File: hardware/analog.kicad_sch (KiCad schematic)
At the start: 11 parts, among them J1 Conn_01x02, U1 ${SIM.PARAMS}, U2 ${SIM.PARAMS}, U3 ${SIM.PARAMS}

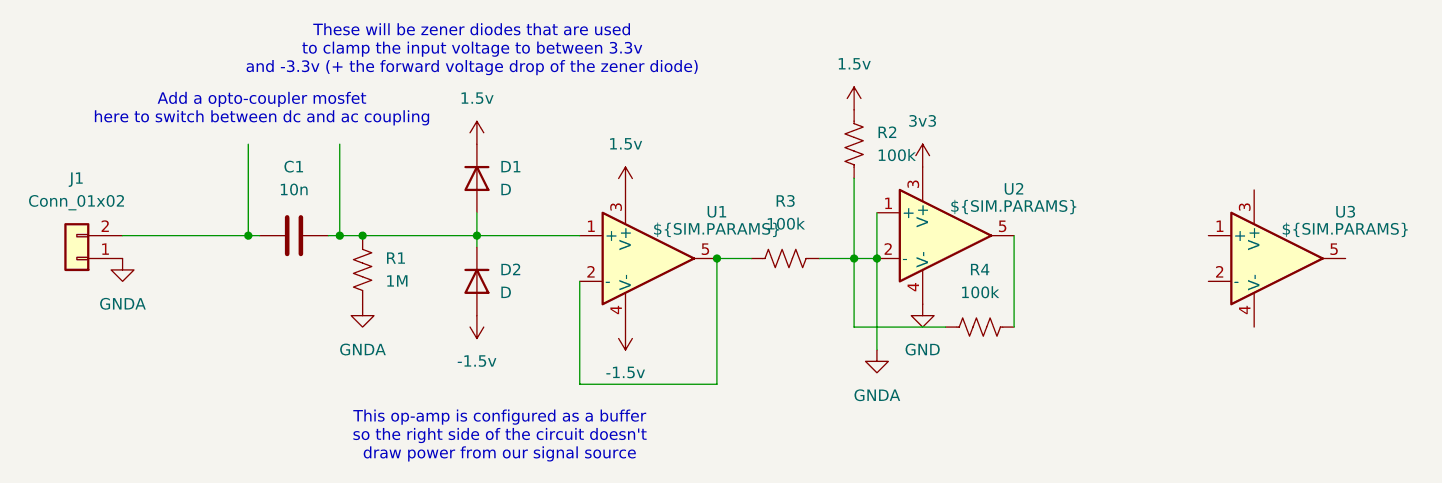
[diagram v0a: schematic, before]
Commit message: feat(hardware): Add 8MB PSRAM Flash
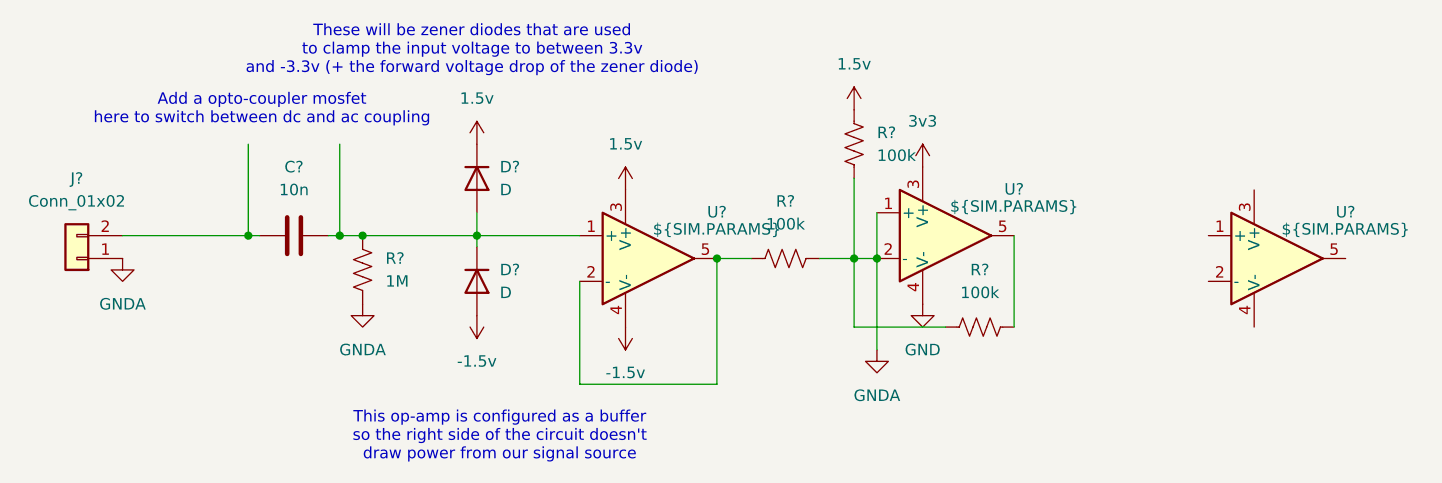
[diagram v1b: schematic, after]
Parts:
- renumbered C1 to C?, D1 to D?, D2 to D?, J1 to J?, R2 to R?, R4 to R?, R3 to R?, R1 to R?, U1 to U?, U3 to U?, U2 to U?
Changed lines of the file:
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@@
 		(dnp no)
 		(fields_autoplaced yes)
-		(property "Reference" "D1"
+		(property "Reference" "D?"
 			(at 81.28 59.6899 90)
 			(effects
@@
 		)
 		(instances
+			(project "RP2350_60QFN_minimal"
+				(path "/94683f5c-9cd9-448e-be96-9792537b5cb8/73c3c5fb-df78-41b9-8072-c8773a39fe38"
+					(reference "D?")
+					(unit 1)
+				)
+			)
 			(project ""
 				(path "/cad06ff6-1510-49dc-9cf8-644755c75ad2"
@@
 		(dnp no)
 		(fields_autoplaced yes)
-		(property "Reference" "#PWR02"
+		(property "Reference" "#PWR?"
 			(at 66.04 81.28 0)
 			(effects
@@
 		)
 		(instances
+			(project "RP2350_60QFN_minimal"
+				(path "/94683f5c-9cd9-448e-be96-9792537b5cb8/73c3c5fb-df78-41b9-8072-c8773a39fe38"
+					(reference "#PWR?")
+					(unit 1)
+				)
+			)
 			(project "analog"
 				(path "/cad06ff6-1510-49dc-9cf8-644755c75ad2"
@@
 		(dnp no)
 		(fields_autoplaced yes)
-		(property "Reference" "#PWR03"
+		(property "Reference" "#PWR?"
 			(at 78.74 60.96 0)
 			(effects
@@
 		)
 		(instances
+			(project "RP2350_60QFN_minimal"
+				(path "/94683f5c-9cd9-448e-be96-9792537b5cb8/73c3c5fb-df78-41b9-8072-c8773a39fe38"
+					(reference "#PWR?")
+					(unit 1)
+				)
+			)
 			(project ""
 				(path "/cad06ff6-1510-49dc-9cf8-644755c75ad2"
@@
 		(dnp no)
 		(fields_autoplaced yes)
-		(property "Reference" "U1"
+		(property "Reference" "U?"
 			(at 105.41 64.6998 0)
 			(effects
@@
 		)
 		(instances
+			(project "RP2350_60QFN_minimal"
+				(path "/94683f5c-9cd9-448e-be96-9792537b5cb8/73c3c5fb-df78-41b9-8072-c8773a39fe38"
+					(reference "U?")
+					(unit 1)
+				)
+			)
 			(project ""
 				(path "/cad06ff6-1510-49dc-9cf8-644755c75ad2"
@@
 		(dnp no)
 		(fields_autoplaced yes)
-		(property "Reference" "U3"
+		(property "Reference" "U?"
 			(at 175.26 64.6998 0)
 			(effects
@@
 		)
 		(instances
+			(project "RP2350_60QFN_minimal"
+				(path "/94683f5c-9cd9-448e-be96-9792537b5cb8/73c3c5fb-df78-41b9-8072-c8773a39fe38"
+					(reference "U?")
+					(unit 1)
+				)
+			)
 			(project "analog"
 				(path "/cad06ff6-1510-49dc-9cf8-644755c75ad2"
@@
 		(dnp no)
 		(fields_autoplaced yes)
-		(property "Reference" "U2"
+		(property "Reference" "U?"
 			(at 138.43 62.1598 0)
 			(effects
@@
 		)
 		(instances
+			(project "RP2350_60QFN_minimal"
+				(path "/94683f5c-9cd9-448e-be96-9792537b5cb8/73c3c5fb-df78-41b9-8072-c8773a39fe38"
+					(reference "U?")
+					(unit 1)
+				)
+			)
 			(project "analog"
 				(path "/cad06ff6-1510-49dc-9cf8-644755c75ad2"
@@
 		(dnp no)
 		(fields_autoplaced yes)
-		(property "Reference" "C1"
+		(property "Reference" "C?"
 			(at 58.42 59.69 90)
 			(effects
@@
 		)
 		(instances
+			(project "RP2350_60QFN_minimal"
+				(path "/94683f5c-9cd9-448e-be96-9792537b5cb8/73c3c5fb-df78-41b9-8072-c8773a39fe38"
+					(reference "C?")
+					(unit 1)
+				)
+			)
 			(project ""
 				(path "/cad06ff6-1510-49dc-9cf8-644755c75ad2"
@@
 		(dnp no)
 		(fields_autoplaced yes)
-		(property "Reference" "#PWR06"
+		(property "Reference" "#PWR?"
 			(at 95.25 73.66 0)
 			(effects
@@
 		)
 		(instances
+			(project "RP2350_60QFN_minimal"
+				(path "/94683f5c-9cd9-448e-be96-9792537b5cb8/73c3c5fb-df78-41b9-8072-c8773a39fe38"
+					(reference "#PWR?")
+					(unit 1)
+				)
+			)
 			(project "analog"
 				(path "/cad06ff6-1510-49dc-9cf8-644755c75ad2"
@@
 		(dnp no)
 		(fields_autoplaced yes)
-		(property "Reference" "R2"
+		(property "Reference" "R?"
 			(at 123.19 55.8799 0)
 			(effects
@@
 		)
 		(instances
+			(project "RP2350_60QFN_minimal"
+				(path "/94683f5c-9cd9-448e-be96-9792537b5cb8/73c3c5fb-df78-41b9-8072-c8773a39fe38"
+					(reference "R?")
+					(unit 1)
+				)
+			)
 			(project ""
 				(path "/cad06ff6-1510-49dc-9cf8-644755c75ad2"
@@
 		(dnp no)
 		(fields_autoplaced yes)
-		(property "Reference" "R4"
+		(property "Reference" "R?"
 			(at 134.62 71.12 90)
 			(effects
@@
 		)
 		(instances
+			(project "RP2350_60QFN_minimal"
+				(path "/94683f5c-9cd9-448e-be96-9792537b5cb8/73c3c5fb-df78-41b9-8072-c8773a39fe38"
+					(reference "R?")
+					(unit 1)
+				)
+			)
 			(project "analog"
 				(path "/cad06ff6-1510-49dc-9cf8-644755c75ad2"
@@
 		(dnp no)
 		(fields_autoplaced yes)
-		(property "Reference" "R3"
+		(property "Reference" "R?"
 			(at 113.03 63.5 90)
 			(effects
@@
 		)
 		(instances
+			(project "RP2350_60QFN_minimal"
+				(path "/94683f5c-9cd9-448e-be96-9792537b5cb8/73c3c5fb-df78-41b9-8072-c8773a39fe38"
+					(reference "R?")
+					(unit 1)
+				)
+			)
 			(project "analog"
 				(path "/cad06ff6-1510-49dc-9cf8-644755c75ad2"
@@
 		(dnp no)
 		(fields_autoplaced yes)
-		(property "Reference" "D2"
+		(property "Reference" "D?"
 			(at 81.28 71.1199 90)
 			(effects
@@
 		)
 		(instances
+			(project "RP2350_60QFN_minimal"
+				(path "/94683f5c-9cd9-448e-be96-9792537b5cb8/73c3c5fb-df78-41b9-8072-c8773a39fe38"
+					(reference "D?")
+					(unit 1)
+				)
+			)
 			(project "analog"
 				(path "/cad06ff6-1510-49dc-9cf8-644755c75ad2"
@@
 		(dnp no)
 		(fields_autoplaced yes)
-		(property "Reference" "R1"
+		(property "Reference" "R?"
 			(at 68.58 69.8499 0)
 			(effects
@@
 		)
 		(instances
+			(project "RP2350_60QFN_minimal"
+				(path "/94683f5c-9cd9-448e-be96-9792537b5cb8/73c3c5fb-df78-41b9-8072-c8773a39fe38"
+					(reference "R?")
+					(unit 1)
+				)
+			)
 			(project ""
 				(path "/cad06ff6-1510-49dc-9cf8-644755c75ad2"
@@
 		(dnp no)
 		(fields_autoplaced yes)
-		(property "Reference" "#PWR08"
+		(property "Reference" "#PWR?"
 			(at 120.65 57.15 0)
 			(effects
@@
 		)
 		(instances
+			(project "RP2350_60QFN_minimal"
+				(path "/94683f5c-9cd9-448e-be96-9792537b5cb8/73c3c5fb-df78-41b9-8072-c8773a39fe38"
+					(reference "#PWR?")
+					(unit 1)
+				)
+			)
 			(project "analog"
 				(path "/cad06ff6-1510-49dc-9cf8-644755c75ad2"
@@
 		(dnp no)
 		(fields_autoplaced yes)
-		(property "Reference" "#PWR010"
+		(property "Reference" "#PWR?"
 			(at 128.27 81.28 0)
 			(effects
@@
 		)
 		(instances
+			(project "RP2350_60QFN_minimal"
+				(path "/94683f5c-9cd9-448e-be96-9792537b5cb8/73c3c5fb-df78-41b9-8072-c8773a39fe38"
+					(reference "#PWR?")
+					(unit 1)
+				)
+			)
 			(project "analog"
 				(path "/cad06ff6-1510-49dc-9cf8-644755c75ad2"
@@
 		(dnp no)
 		(fields_autoplaced yes)
-		(property "Reference" "#PWR09"
+		(property "Reference" "#PWR?"
 			(at 128.27 63.5 0)
 			(effects
@@
 		)
 		(instances
+			(project "RP2350_60QFN_minimal"
+				(path "/94683f5c-9cd9-448e-be96-9792537b5cb8/73c3c5fb-df78-41b9-8072-c8773a39fe38"
+					(reference "#PWR?")
+					(unit 1)
+				)
+			)
 			(project "analog"
 				(path "/cad06ff6-1510-49dc-9cf8-644755c75ad2"
@@
 		(dnp no)
 		(fields_autoplaced yes)
-		(property "Reference" "#PWR04"
+		(property "Reference" "#PWR?"
 			(at 78.74 72.39 0)
 			(effects
@@
 		)
 		(instances
+			(project "RP2350_60QFN_minimal"
+				(path "/94683f5c-9cd9-448e-be96-9792537b5cb8/73c3c5fb-df78-41b9-8072-c8773a39fe38"
+					(reference "#PWR?")
+					(unit 1)
+				)
+			)
 			(project ""
 				(path "/cad06ff6-1510-49dc-9cf8-644755c75ad2"
@@
 		(dnp no)
 		(fields_autoplaced yes)
-		(property "Reference" "#PWR01"
+		(property "Reference" "#PWR?"
 			(at 39.37 76.2 0)
 			(effects
@@
 		)
 		(instances
+			(project "RP2350_60QFN_minimal"
+				(path "/94683f5c-9cd9-448e-be96-9792537b5cb8/73c3c5fb-df78-41b9-8072-c8773a39fe38"
+					(reference "#PWR?")
+					(unit 1)
+				)
+			)
 			(project ""
 				(path "/cad06ff6-1510-49dc-9cf8-644755c75ad2"
@@
 		(dnp no)
 		(fields_autoplaced yes)
-		(property "Reference" "J1"
+		(property "Reference" "J?"
 			(at 34.29 60.96 0)
 			(effects
@@
 		)
 		(instances
+			(project "RP2350_60QFN_minimal"
+				(path "/94683f5c-9cd9-448e-be96-9792537b5cb8/73c3c5fb-df78-41b9-8072-c8773a39fe38"
+					(reference "J?")
+					(unit 1)
+				)
+			)
 			(project ""
 				(path "/cad06ff6-1510-49dc-9cf8-644755c75ad2"
@@
 		(dnp no)
 		(fields_autoplaced yes)
-		(property "Reference" "#PWR05"
+		(property "Reference" "#PWR?"
 			(at 95.25 66.04 0)
 			(effects
@@
 		)
 		(instances
+			(project "RP2350_60QFN_minimal"
+				(path "/94683f5c-9cd9-448e-be96-9792537b5cb8/73c3c5fb-df78-41b9-8072-c8773a39fe38"
+					(reference "#PWR?")
+					(unit 1)
+				)
+			)
 			(project "analog"
 				(path "/cad06ff6-1510-49dc-9cf8-644755c75ad2"
@@
 		(dnp no)
 		(fields_autoplaced yes)
-		(property "Reference" "#PWR07"
+		(property "Reference" "#PWR?"
 			(at 123.19 86.36 0)
 			(effects
@@
 		)
 		(instances
+			(project "RP2350_60QFN_minimal"
+				(path "/94683f5c-9cd9-448e-be96-9792537b5cb8/73c3c5fb-df78-41b9-8072-c8773a39fe38"
+					(reference "#PWR?")
+					(unit 1)
+				)
+			)
 			(project "analog"
 				(path "/cad06ff6-1510-49dc-9cf8-644755c75ad2"

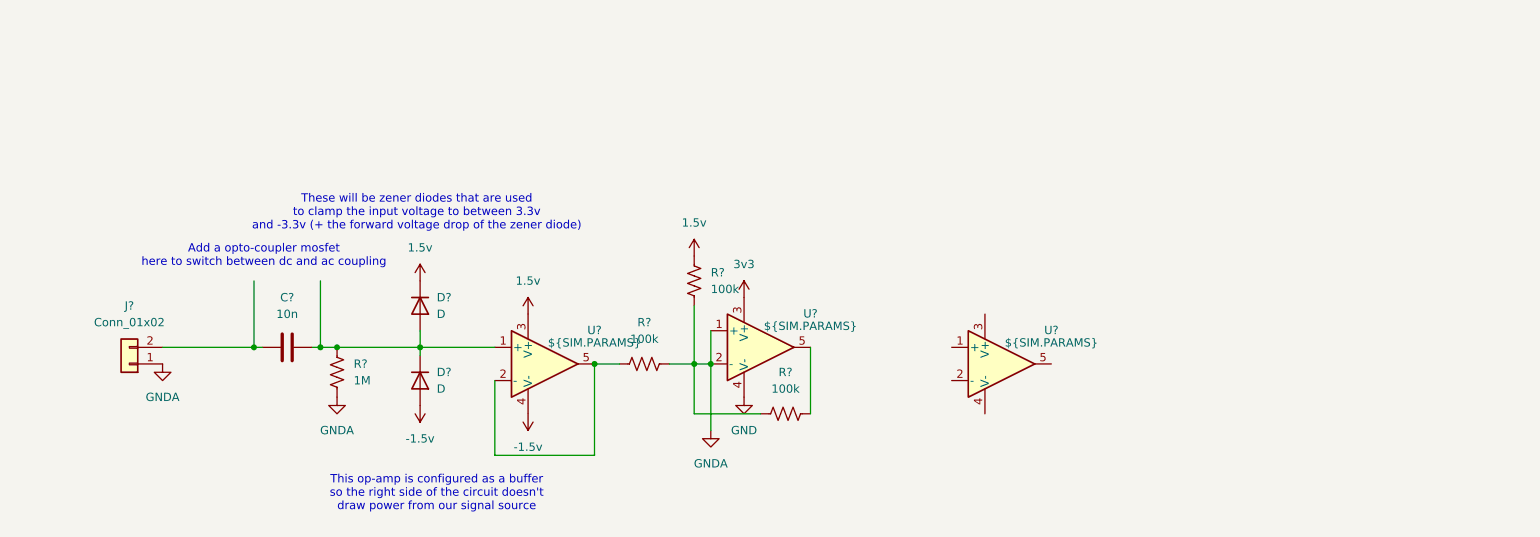
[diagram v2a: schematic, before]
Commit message: added heirarchical labels for analog block
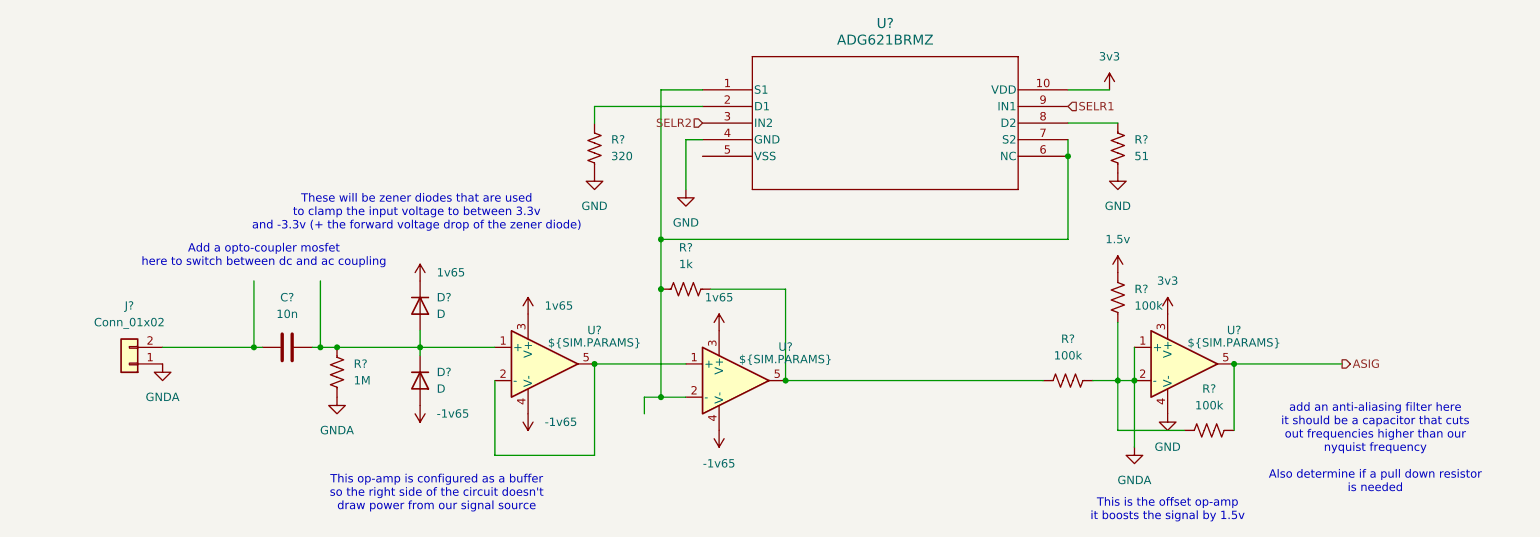
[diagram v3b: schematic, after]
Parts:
- added R?: 320, symbol Device:R_US
- added R?: 1k, symbol Device:R_US
- added R?: 51, symbol Device:R_US
- added U?: ADG621BRMZ, RM_10_ADI, symbol ADG621BRMZ (switch):ADG621BRMZ
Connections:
- net -1.5v is gone; now on net -1v65: D?.2 (A), U?.4 (V-)
- net 1.5v: no longer D?.1 (K), U?.3 (V+)
- net 3v3: now also U?.10 (VDD)
- net GND: now also R?.1, R?.1, U?.4 (GND)
- net at U?.2 (-), U?.5: now also U?.1 (+); no longer R?.2
- net at U?.2 (-): now also R?.1, U?.1 (S1), U?.6 (NC), U?.7 (S2)
- net 1v65: now reaches U?.3 (V+)
- net 1v65: now also D?.1 (K), U?.3 (V+)
- net -1v65: now reaches U?.4 (V-)
- net at U?.5: now also R?.2, R?.2
- net ASIG: now reaches R?.1, U?.5
- new net: R?.2, U?.2 (D1)
- new net: R?.2, U?.8 (D2)
- new net SELR1: U?.9 (IN1)
- new net SELR2: U?.3 (IN2)
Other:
- note added: "This is the offset op-amp it boosts the signal by 1.5v"
- note added: "add an anti-aliasing filter here it should be a capacitor that cuts out frequencies higher than our nyquist frequency Also determine if a pull down resistor is needed"
- moved on the sheet: R?, U?

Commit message: merging stuff
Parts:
- gave numbers to parts that had none: 15
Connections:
- net GND: no longer U4.4 (GND)
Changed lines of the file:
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@@
 		(dnp no)
 		(fields_autoplaced yes)
-		(property "Reference" "#PWR?"
+		(property "Reference" "#PWR014"
 			(at 124.46 68.58 0)
 			(effects
@@
 		(dnp no)
 		(fields_autoplaced yes)
-		(property "Reference" "D?"
+		(property "Reference" "D1"
 			(at 81.28 59.6899 90)
 			(effects
@@
 		(dnp no)
 		(fields_autoplaced yes)
-		(property "Reference" "#PWR?"
+		(property "Reference" "#PWR02"
 			(at 66.04 81.28 0)
 			(effects
@@
 		(dnp no)
 		(fields_autoplaced yes)
-		(property "Reference" "R?"
+		(property "Reference" "R7"
 			(at 107.95 35.5599 0)
 			(effects
@@
 		(dnp no)
 		(fields_autoplaced yes)
-		(property "Reference" "#PWR?"
+		(property "Reference" "#PWR03"
 			(at 78.74 60.96 0)
 			(effects
@@
 		(dnp no)
 		(fields_autoplaced yes)
-		(property "Reference" "U?"
+		(property "Reference" "U1"
 			(at 105.41 64.6998 0)
 			(effects
@@
 		(dnp no)
 		(fields_autoplaced yes)
-		(property "Reference" "U?"
+		(property "Reference" "U3"
 			(at 134.62 67.2398 0)
 			(effects
@@
 		(dnp no)
 		(fields_autoplaced yes)
-		(property "Reference" "U?"
+		(property "Reference" "U2"
 			(at 203.2 64.6998 0)
 			(effects
@@
 		(dnp no)
 		(fields_autoplaced yes)
-		(property "Reference" "C?"
+		(property "Reference" "C1"
 			(at 58.42 59.69 90)
 			(effects
@@
 		(dnp no)
 		(fields_autoplaced yes)
-		(property "Reference" "#PWR?"
+		(property "Reference" "#PWR06"
 			(at 95.25 73.66 0)
 			(effects
@@
 		(dnp no)
 		(fields_autoplaced yes)
-		(property "Reference" "R?"
+		(property "Reference" "R6"
 			(at 119.38 52.07 90)
 			(effects
@@
 		(dnp no)
 		(fields_autoplaced yes)
-		(property "Reference" "R?"
+		(property "Reference" "R2"
 			(at 187.96 58.4199 0)
 			(effects
@@
 		(dnp no)
 		(fields_autoplaced yes)
-		(property "Reference" "R?"
+		(property "Reference" "R4"
 			(at 199.39 73.66 90)
 			(effects
@@
 		(dnp no)
 		(fields_autoplaced yes)
-		(property "Reference" "#PWR?"
+		(property "Reference" "#PWR015"
 			(at 124.46 76.2 0)
 			(effects
@@
 		(dnp no)
 		(fields_autoplaced yes)
-		(property "Reference" "R?"
+		(property "Reference" "R3"
 			(at 177.8 66.04 90)
 			(effects
@@
 		(dnp no)
 		(fields_autoplaced yes)
-		(property "Reference" "D?"
+		(property "Reference" "D2"
 			(at 81.28 71.1199 90)
 			(effects
@@
 		(dnp no)
 		(fields_autoplaced yes)
-		(property "Reference" "R?"
+		(property "Reference" "R1"
 			(at 68.58 69.8499 0)
 			(effects
@@
 		(dnp no)
 		(fields_autoplaced yes)
-		(property "Reference" "#PWR?"
+		(property "Reference" "#PWR016"
 			(at 105.41 46.99 0)
 			(effects
@@
 		(dnp no)
 		(fields_autoplaced yes)
-		(property "Reference" "R?"
+		(property "Reference" "R8"
 			(at 187.96 35.5599 0)
 			(effects
@@
 		(dnp no)
 		(fields_autoplaced yes)
-		(property "Reference" "#PWR?"
+		(property "Reference" "#PWR08"
 			(at 185.42 59.69 0)
 			(effects
@@
 		(dnp no)
 		(fields_autoplaced yes)
-		(property "Reference" "#PWR?"
+		(property "Reference" "#PWR017"
 			(at 185.42 46.99 0)
 			(effects
@@
 		(dnp no)
 		(fields_autoplaced yes)
-		(property "Reference" "#PWR?"
+		(property "Reference" "#PWR010"
 			(at 193.04 83.82 0)
 			(effects
@@
 		(dnp no)
 		(fields_autoplaced yes)
-		(property "Reference" "U?"
+		(property "Reference" "U4"
 			(at 149.86 17.78 0)
 			(effects
@@
 	)
 	(symbol
-		(lib_id "power:GND")
-		(at 119.38 43.18 0)
-		(unit 1)
-		(exclude_from_sim no)
-		(in_bom yes)
-		(on_board yes)
-		(dnp no)
-		(fields_autoplaced yes)
-		(property "Reference" "#PWR?"
-			(at 119.38 49.53 0)
-			(effects
-				(font
-					(size 1.27 1.27)
-				)
-				(hide yes)
-			)
-		)
-		(property "Value" "GND"
-			(at 119.38 48.26 0)
-			(effects
-				(font
-					(size 1.27 1.27)
-				)
-			)
-		)
-		(property "Footprint" ""
-			(at 119.38 43.18 0)
-			(effects
-				(font
-					(size 1.27 1.27)
-				)
-				(hide yes)
-			)
-		)
-		(property "Datasheet" ""
-			(at 119.38 43.18 0)
-			(effects
-				(font
-					(size 1.27 1.27)
-				)
-				(hide yes)
-			)
-		)
-		(property "Description" "Power symbol creates a global label with name \"GND\" , ground"
-			(at 119.38 43.18 0)
-			(effects
-				(font
-					(size 1.27 1.27)
-				)
-				(hide yes)
-			)
-		)
-		(pin "1"
-		)
-		(instances
-			(project "RP2350_60QFN_minimal"
-				(path "/94683f5c-9cd9-448e-be96-9792537b5cb8/73c3c5fb-df78-41b9-8072-c8773a39fe38"
-					(reference "#PWR?")
-					(unit 1)
-				)
-			)
-			(project "analog"
-				(path "/cad06ff6-1510-49dc-9cf8-644755c75ad2"
-					(reference "#PWR013")
-					(unit 1)
-				)
-			)
-		)
-	)
-	(symbol
 		(lib_id "power:VDC")
 		(at 193.04 62.23 0)
@@
 		(dnp no)
 		(fields_autoplaced yes)
-		(property "Reference" "#PWR?"
+		(property "Reference" "#PWR09"
 			(at 193.04 66.04 0)
 			(effects
@@
 		(dnp no)
 		(fields_autoplaced yes)
-		(property "Reference" "#PWR?"
+		(property "Reference" "#PWR04"
 			(at 78.74 72.39 0)
 			(effects
@@
 		(dnp no)
 		(fields_autoplaced yes)
-		(property "Reference" "#PWR?"
+		(property "Reference" "#PWR01"
 			(at 39.37 76.2 0)
 			(effects
@@
 		(dnp no)
 		(fields_autoplaced yes)
-		(property "Reference" "J?"
+		(property "Reference" "J1"
 			(at 34.29 60.96 0)
 			(effects
@@
 		(dnp no)
 		(fields_autoplaced yes)
-		(property "Reference" "#PWR?"
+		(property "Reference" "#PWR05"
 			(at 95.25 66.04 0)
 			(effects
@@
 		(dnp no)
 		(fields_autoplaced yes)
-		(property "Reference" "#PWR?"
+		(property "Reference" "#PWR07"
 			(at 187.96 88.9 0)
 			(effects
@@
 		(dnp no)
 		(fields_autoplaced yes)
-		(property "Reference" "#PWR?"
+		(property "Reference" "#PWR012"
 			(at 184.15 31.75 0)
 			(effects
